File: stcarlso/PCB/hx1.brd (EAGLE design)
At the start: 44.1 x 14 mm, 5 parts, among them J1 SMA_EDGE, J2 CTRL, U1 HX1

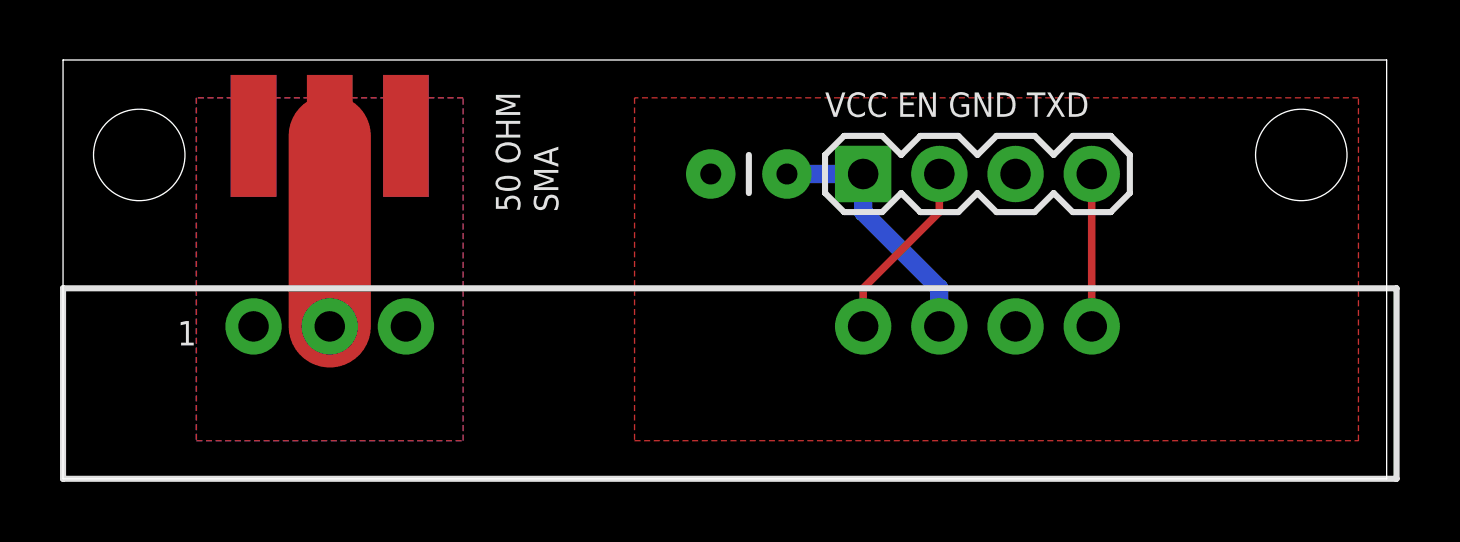
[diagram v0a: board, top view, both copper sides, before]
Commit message: Update PCB to include pads for RC filter (values TBD)
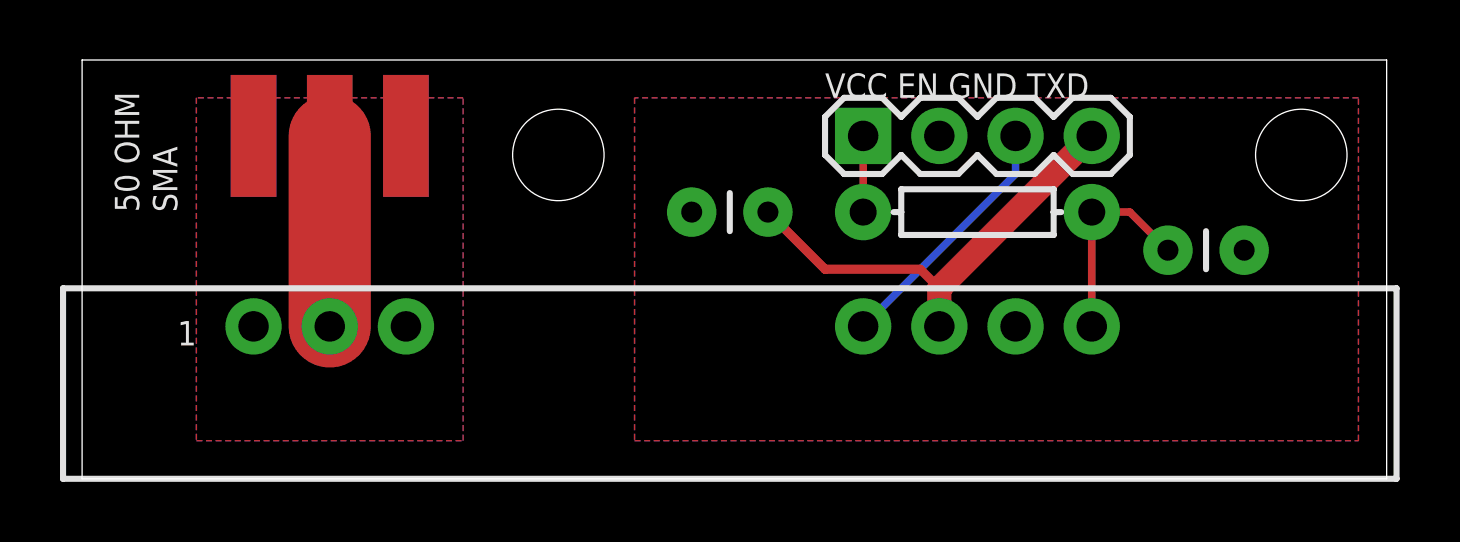
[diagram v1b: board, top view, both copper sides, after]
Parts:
- added C2: TBD, SparkFun-Passives:CAP-PTH-SMALL
- added R1: TBD, SparkFun-Passives:AXIAL-0.3
- moved C1 1.42 mm to (23.5, 8.89)
- moved J2 1.27 mm to (26.7, 11.4)
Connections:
- new net TXF: C2.1, R1.P$1, U1.7
- net EN: now also J2.3; no longer J2.2
- net GND: now also C2.2, J2.2; no longer J2.3
- net TXD: now also J2.1, R1.P$2; no longer J2.4, U1.7
- net VCC: now also J2.4; no longer J2.1
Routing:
- net TXF: track 0.00 -> 6.88 mm
- net VCC: track 8.67 -> 15.2 mm
- net TXD: track 5.08 -> 2.54 mm
- net EN: track 6.13 -> 8.45 mm
- added copper zone on layer 16, net GND
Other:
- board size 44.1 x 14 mm -> 43.5 x 14 mm
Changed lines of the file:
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@@
 <board>
 <plain>
-<wire x1="0" y1="0" x2="44.12" y2="0" width="0" layer="20"/>
+<wire x1="0.635" y1="0" x2="44.12" y2="0" width="0" layer="20"/>
 <wire x1="44.12" y1="0" x2="44.12" y2="13.96" width="0" layer="20"/>
-<wire x1="44.12" y1="13.96" x2="0" y2="13.96" width="0" layer="20"/>
-<wire x1="0" y1="13.96" x2="0" y2="0" width="0" layer="20"/>
-<text x="25.4" y="12.065" size="0.8128" layer="21">VCC EN GND TXD</text>
-<text x="43.18" y="6.985" size="1.27" layer="22" rot="MR0">HAB Project, Microsoft Maker Garage</text>
-<text x="43.18" y="1.905" size="1.27" layer="22" rot="MR0">Revision A, ~STCARLSO</text>
-<text x="15.24" y="8.89" size="0.8128" layer="21" rot="R90">50 OHM</text>
-<text x="16.51" y="8.89" size="0.8128" layer="21" rot="R90">SMA</text>
+<wire x1="44.12" y1="13.96" x2="0.635" y2="13.96" width="0" layer="20"/>
+<wire x1="0.635" y1="13.96" x2="0.635" y2="0" width="0" layer="20"/>
+<text x="25.4" y="12.7" size="0.8128" layer="21">VCC EN GND TXD</text>
+<text x="43.18" y="2.54" size="1.27" layer="22" rot="MR0">HAB Project, Microsoft Maker Garage</text>
+<text x="43.18" y="0.635" size="1.27" layer="22" rot="MR0">Revision A, ~STCARLSO</text>
+<text x="2.54" y="8.89" size="0.8128" layer="21" rot="R90">50 OHM</text>
+<text x="3.81" y="8.89" size="0.8128" layer="21" rot="R90">SMA</text>
 <text x="3.81" y="4.445" size="0.8128" layer="21">1</text>
 <hole x="41.275" y="10.795" drill="3.048"/>
-<hole x="2.54" y="10.795" drill="3.048"/>
+<hole x="16.51" y="10.795" drill="3.048"/>
 </plain>
 <attributes>
@@
 </element>
 <element name="J1" library="SparkFun-Connectors" package="SMA-EDGE" value="SMA_EDGE" x="6.35" y="11.43"/>
-<element name="J2" library="SparkFun-Connectors" package="1X04" value="CTRL" x="26.67" y="10.16" smashed="yes">
-<attribute name="VALUE" x="37.465" y="8.89" size="1.27" layer="27" rot="R90"/>
+<element name="J2" library="SparkFun-Connectors" package="1X04" value="CTRL" x="26.67" y="11.43" smashed="yes">
+<attribute name="VALUE" x="20.32" y="10.795" size="1.27" layer="27"/>
 </element>
 <element name="U1" library="HAB" package="1X12" value="HX1" x="6.35" y="5.08" smashed="yes">
-<attribute name="VALUE" x="1.27" y="0.635" size="1.27" layer="27"/>
-</element>
-<element name="C1" library="SparkFun-Passives" package="CAP-PTH-SMALL" value="0.1u" x="24.13" y="10.16" smashed="yes" rot="R180">
-<attribute name="VALUE" x="23.876" y="12.319" size="0.8128" layer="27" rot="R180"/>
-</element>
+<attribute name="VALUE" x="1.905" y="0.635" size="1.27" layer="27"/>
+</element>
+<element name="C1" library="SparkFun-Passives" package="CAP-PTH-SMALL" value="0.1u" x="23.495" y="8.89" smashed="yes" rot="R180">
+<attribute name="VALUE" x="23.241" y="7.874" size="0.8128" layer="27" rot="R180"/>
+</element>
+<element name="R1" library="SparkFun-Passives" package="AXIAL-0.3" value="TBD" x="30.48" y="8.89" smashed="yes" rot="R180"/>
+<element name="C2" library="SparkFun-Passives" package="CAP-PTH-SMALL" value="TBD" x="36.83" y="7.62" smashed="yes"/>
 </elements>
 <signals>
@@
 <contactref element="U1" pad="1"/>
 <contactref element="U1" pad="3"/>
-<polygon width="0.254" layer="16" isolate="0.3048">
+<polygon width="0.254" layer="16" isolate="0.4064">
 <vertex x="4.445" y="12.7"/>
 <vertex x="4.445" y="1.27"/>
@@
 <vertex x="13.335" y="12.7"/>
 </polygon>
-<polygon width="0.254" layer="1" isolate="0.3048">
+<polygon width="0.254" layer="1" isolate="0.4064">
 <vertex x="4.445" y="12.7"/>
 <vertex x="4.445" y="1.27"/>
@@
 <signal name="EN">
 <contactref element="U1" pad="4"/>
-<contactref element="J2" pad="2"/>
-<wire x1="26.67" y1="5.08" x2="26.67" y2="6.35" width="0.254" layer="1"/>
-<wire x1="26.67" y1="6.35" x2="29.21" y2="8.89" width="0.254" layer="1"/>
-<wire x1="29.21" y1="8.89" x2="29.21" y2="10.16" width="0.254" layer="1"/>
+<contactref element="J2" pad="3"/>
+<wire x1="31.75" y1="11.43" x2="31.75" y2="10.16" width="0.254" layer="16"/>
+<wire x1="31.75" y1="10.16" x2="26.67" y2="5.08" width="0.254" layer="16"/>
 </signal>
 <signal name="VCC">
 <contactref element="U1" pad="5"/>
-<contactref element="J2" pad="1"/>
-<wire x1="29.21" y1="5.08" x2="29.21" y2="6.35" width="0.6096" layer="16"/>
-<wire x1="29.21" y1="6.35" x2="26.67" y2="8.89" width="0.6096" layer="16"/>
-<wire x1="26.67" y1="8.89" x2="26.67" y2="10.16" width="0.6096" layer="16"/>
 <contactref element="C1" pad="1"/>
-<wire x1="24.13" y1="10.16" x2="26.67" y2="10.16" width="0.6096" layer="16"/>
-</signal>
-<signal name="TXD">
-<contactref element="U1" pad="7"/>
 <contactref element="J2" pad="4"/>
-<wire x1="34.29" y1="10.16" x2="34.29" y2="5.08" width="0.254" layer="1"/>
+<wire x1="34.29" y1="11.43" x2="29.21" y2="6.35" width="0.8128" layer="1"/>
+<wire x1="29.21" y1="6.35" x2="29.21" y2="5.08" width="0.8128" layer="1"/>
+<wire x1="29.21" y1="6.35" x2="28.575" y2="6.985" width="0.3048" layer="1"/>
+<wire x1="28.575" y1="6.985" x2="25.4" y2="6.985" width="0.3048" layer="1"/>
+<wire x1="25.4" y1="6.985" x2="23.495" y2="8.89" width="0.3048" layer="1"/>
 </signal>
 <signal name="GND">
 <contactref element="U1" pad="6"/>
-<contactref element="J2" pad="3"/>
 <polygon width="0.254" layer="1" isolate="0.3048">
 <vertex x="19.05" y="12.7"/>
@@
 </polygon>
 <contactref element="C1" pad="2"/>
+<contactref element="C2" pad="2"/>
+<contactref element="J2" pad="2"/>
+<polygon width="0.254" layer="16" isolate="0.3048">
+<vertex x="19.05" y="12.7"/>
+<vertex x="19.05" y="1.27"/>
+<vertex x="43.18" y="1.27"/>
+<vertex x="43.18" y="12.7"/>
+</polygon>
+</signal>
+<signal name="TXF">
+<contactref element="R1" pad="P$1"/>
+<contactref element="C2" pad="1"/>
+<contactref element="U1" pad="7"/>
+<wire x1="34.29" y1="8.89" x2="35.56" y2="8.89" width="0.254" layer="1"/>
+<wire x1="35.56" y1="8.89" x2="36.83" y2="7.62" width="0.254" layer="1"/>
+<wire x1="34.29" y1="8.89" x2="34.29" y2="5.08" width="0.254" layer="1"/>
+</signal>
+<signal name="TXD">
+<contactref element="R1" pad="P$2"/>
+<contactref element="J2" pad="1"/>
+<wire x1="26.67" y1="11.43" x2="26.67" y2="8.89" width="0.254" layer="1"/>
 </signal>
 </signals>

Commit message: Update PCB footprint of HX1 with tighter dimensions
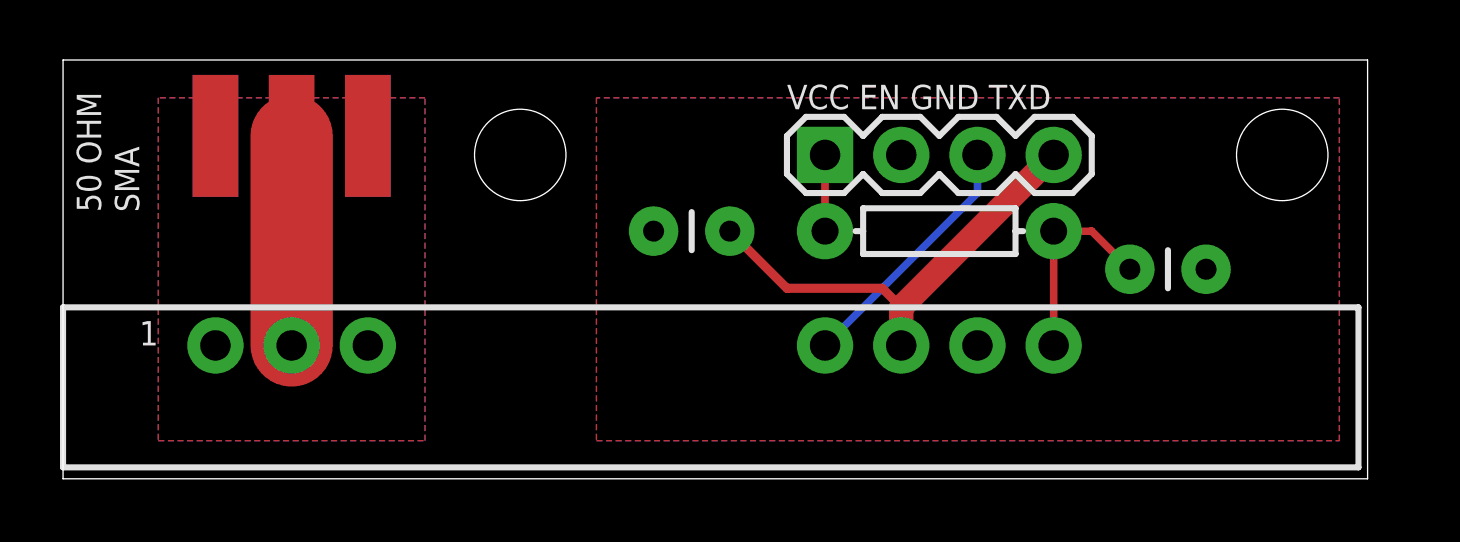
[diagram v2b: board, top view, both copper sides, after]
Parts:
- moved J2 1.42 mm to (25.4, 10.8)
- moved C1 1.42 mm to (22.2, 8.26)
- moved R1 1.42 mm to (29.2, 8.26)
- moved U1 1.42 mm to (5.08, 4.45)
- moved C2 1.42 mm to (35.6, 6.99)
- moved FRAME1 1.27 mm to (-1.27, 15.2)
- moved J1 1.27 mm to (5.08, 11.4)
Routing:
- net RFOUT: track 6.35 -> 6.98 mm
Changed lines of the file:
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@@
 <board>
 <plain>
-<wire x1="0.635" y1="0" x2="44.12" y2="0" width="0" layer="20"/>
-<wire x1="44.12" y1="0" x2="44.12" y2="13.96" width="0" layer="20"/>
-<wire x1="44.12" y1="13.96" x2="0.635" y2="13.96" width="0" layer="20"/>
-<wire x1="0.635" y1="13.96" x2="0.635" y2="0" width="0" layer="20"/>
-<text x="25.4" y="12.7" size="0.8128" layer="21">VCC EN GND TXD</text>
-<text x="43.18" y="2.54" size="1.27" layer="22" rot="MR0">HAB Project, Microsoft Maker Garage</text>
-<text x="43.18" y="0.635" size="1.27" layer="22" rot="MR0">Revision A, ~STCARLSO</text>
-<text x="2.54" y="8.89" size="0.8128" layer="21" rot="R90">50 OHM</text>
-<text x="3.81" y="8.89" size="0.8128" layer="21" rot="R90">SMA</text>
-<text x="3.81" y="4.445" size="0.8128" layer="21">1</text>
-<hole x="41.275" y="10.795" drill="3.048"/>
-<hole x="16.51" y="10.795" drill="3.048"/>
+<wire x1="0" y1="0" x2="43.485" y2="0" width="0" layer="20"/>
+<wire x1="43.485" y1="0" x2="43.485" y2="13.96" width="0" layer="20"/>
+<wire x1="43.485" y1="13.96" x2="0" y2="13.96" width="0" layer="20"/>
+<wire x1="0" y1="13.96" x2="0" y2="0" width="0" layer="20"/>
+<text x="24.13" y="12.319" size="0.8128" layer="21">VCC EN GND TXD</text>
+<text x="41.91" y="2.54" size="1.27" layer="22" rot="MR0">HAB Project, Microsoft Maker Garage</text>
+<text x="41.91" y="0.635" size="1.27" layer="22" rot="MR0">Revision A, ~STCARLSO</text>
+<text x="1.27" y="8.89" size="0.8128" layer="21" rot="R90">50 OHM</text>
+<text x="2.54" y="8.89" size="0.8128" layer="21" rot="R90">SMA</text>
+<text x="2.54" y="4.445" size="0.8128" layer="21">1</text>
+<hole x="40.64" y="10.795" drill="3.048"/>
+<hole x="15.24" y="10.795" drill="3.048"/>
 </plain>
 <attributes>
@@
 </autorouter>
 <elements>
-<element name="FRAME1" library="SparkFun-Aesthetics" package="DUMMY" value="" x="0" y="15.24">
-<attribute name="VERSION" value="v01" x="0" y="15.24" size="1.778" layer="27" display="off"/>
-<attribute name="DESIGNER" value="Nobody" x="0" y="15.24" size="1.778" layer="27" display="off"/>
-</element>
-<element name="J1" library="SparkFun-Connectors" package="SMA-EDGE" value="SMA_EDGE" x="6.35" y="11.43"/>
-<element name="J2" library="SparkFun-Connectors" package="1X04" value="CTRL" x="26.67" y="11.43" smashed="yes">
-<attribute name="VALUE" x="20.32" y="10.795" size="1.27" layer="27"/>
-</element>
-<element name="U1" library="HAB" package="1X12" value="HX1" x="6.35" y="5.08" smashed="yes">
-<attribute name="VALUE" x="1.905" y="0.635" size="1.27" layer="27"/>
-</element>
-<element name="C1" library="SparkFun-Passives" package="CAP-PTH-SMALL" value="0.1u" x="23.495" y="8.89" smashed="yes" rot="R180">
-<attribute name="VALUE" x="23.241" y="7.874" size="0.8128" layer="27" rot="R180"/>
-</element>
-<element name="R1" library="SparkFun-Passives" package="AXIAL-0.3" value="TBD" x="30.48" y="8.89" smashed="yes" rot="R180"/>
-<element name="C2" library="SparkFun-Passives" package="CAP-PTH-SMALL" value="TBD" x="36.83" y="7.62" smashed="yes"/>
+<element name="FRAME1" library="SparkFun-Aesthetics" package="DUMMY" value="" x="-1.27" y="15.24">
+<attribute name="VERSION" value="v01" x="-1.27" y="15.24" size="1.778" layer="27" display="off"/>
+<attribute name="DESIGNER" value="Nobody" x="-1.27" y="15.24" size="1.778" layer="27" display="off"/>
+</element>
+<element name="J1" library="SparkFun-Connectors" package="SMA-EDGE" value="SMA_EDGE" x="5.08" y="11.43"/>
+<element name="J2" library="SparkFun-Connectors" package="1X04" value="CTRL" x="25.4" y="10.795" smashed="yes">
+<attribute name="VALUE" x="19.05" y="10.16" size="1.27" layer="27"/>
+</element>
+<element name="U1" library="HAB" package="1X12" value="HX1" x="5.08" y="4.445" smashed="yes">
+<attribute name="VALUE" x="0.635" y="1.27" size="1.27" layer="27"/>
+</element>
+<element name="C1" library="SparkFun-Passives" package="CAP-PTH-SMALL" value="0.1u" x="22.225" y="8.255" smashed="yes" rot="R180">
+<attribute name="VALUE" x="21.971" y="7.239" size="0.8128" layer="27" rot="R180"/>
+</element>
+<element name="R1" library="SparkFun-Passives" package="AXIAL-0.3" value="TBD" x="29.21" y="8.255" smashed="yes" rot="R180"/>
+<element name="C2" library="SparkFun-Passives" package="CAP-PTH-SMALL" value="TBD" x="35.56" y="6.985" smashed="yes"/>
 </elements>
 <signals>
@@
 <contactref element="J1" pad="SIG"/>
 <contactref element="U1" pad="2"/>
-<wire x1="8.89" y1="11.43" x2="8.89" y2="5.08" width="2.7432" layer="1"/>
+<wire x1="7.62" y1="11.43" x2="7.62" y2="4.445" width="2.7432" layer="1"/>
 </signal>
 <signal name="RFGND">
@@
 <contactref element="U1" pad="3"/>
 <polygon width="0.254" layer="16" isolate="0.4064">
-<vertex x="4.445" y="12.7"/>
-<vertex x="4.445" y="1.27"/>
-<vertex x="13.335" y="1.27"/>
-<vertex x="13.335" y="12.7"/>
+<vertex x="3.175" y="12.7"/>
+<vertex x="3.175" y="1.27"/>
+<vertex x="12.065" y="1.27"/>
+<vertex x="12.065" y="12.7"/>
 </polygon>
 <polygon width="0.254" layer="1" isolate="0.4064">
-<vertex x="4.445" y="12.7"/>
-<vertex x="4.445" y="1.27"/>
-<vertex x="13.335" y="1.27"/>
-<vertex x="13.335" y="12.7"/>
+<vertex x="3.175" y="12.7"/>
+<vertex x="3.175" y="1.27"/>
+<vertex x="12.065" y="1.27"/>
+<vertex x="12.065" y="12.7"/>
 </polygon>
 </signal>
@@
 <contactref element="U1" pad="4"/>
 <contactref element="J2" pad="3"/>
-<wire x1="31.75" y1="11.43" x2="31.75" y2="10.16" width="0.254" layer="16"/>
-<wire x1="31.75" y1="10.16" x2="26.67" y2="5.08" width="0.254" layer="16"/>
+<wire x1="30.48" y1="10.795" x2="30.48" y2="9.525" width="0.254" layer="16"/>
+<wire x1="30.48" y1="9.525" x2="25.4" y2="4.445" width="0.254" layer="16"/>
 </signal>
 <signal name="VCC">
@@
 <contactref element="C1" pad="1"/>
 <contactref element="J2" pad="4"/>
-<wire x1="34.29" y1="11.43" x2="29.21" y2="6.35" width="0.8128" layer="1"/>
-<wire x1="29.21" y1="6.35" x2="29.21" y2="5.08" width="0.8128" layer="1"/>
-<wire x1="29.21" y1="6.35" x2="28.575" y2="6.985" width="0.3048" layer="1"/>
-<wire x1="28.575" y1="6.985" x2="25.4" y2="6.985" width="0.3048" layer="1"/>
-<wire x1="25.4" y1="6.985" x2="23.495" y2="8.89" width="0.3048" layer="1"/>
+<wire x1="33.02" y1="10.795" x2="27.94" y2="5.715" width="0.8128" layer="1"/>
+<wire x1="27.94" y1="5.715" x2="27.94" y2="4.445" width="0.8128" layer="1"/>
+<wire x1="27.94" y1="5.715" x2="27.305" y2="6.35" width="0.3048" layer="1"/>
+<wire x1="27.305" y1="6.35" x2="24.13" y2="6.35" width="0.3048" layer="1"/>
+<wire x1="24.13" y1="6.35" x2="22.225" y2="8.255" width="0.3048" layer="1"/>
 </signal>
 <signal name="GND">
 <contactref element="U1" pad="6"/>
 <polygon width="0.254" layer="1" isolate="0.3048">
-<vertex x="19.05" y="12.7"/>
-<vertex x="19.05" y="1.27"/>
-<vertex x="43.18" y="1.27"/>
-<vertex x="43.18" y="12.7"/>
+<vertex x="17.78" y="12.7"/>
+<vertex x="17.78" y="1.27"/>
+<vertex x="42.545" y="1.27"/>
+<vertex x="42.545" y="12.7"/>
 </polygon>
 <contactref element="C1" pad="2"/>
@@
 <contactref element="J2" pad="2"/>
 <polygon width="0.254" layer="16" isolate="0.3048">
-<vertex x="19.05" y="12.7"/>
-<vertex x="19.05" y="1.27"/>
-<vertex x="43.18" y="1.27"/>
-<vertex x="43.18" y="12.7"/>
+<vertex x="17.78" y="12.7"/>
+<vertex x="17.78" y="1.27"/>
+<vertex x="42.545" y="1.27"/>
+<vertex x="42.545" y="12.7"/>
 </polygon>
 </signal>
@@
 <contactref element="C2" pad="1"/>
 <contactref element="U1" pad="7"/>
-<wire x1="34.29" y1="8.89" x2="35.56" y2="8.89" width="0.254" layer="1"/>
-<wire x1="35.56" y1="8.89" x2="36.83" y2="7.62" width="0.254" layer="1"/>
-<wire x1="34.29" y1="8.89" x2="34.29" y2="5.08" width="0.254" layer="1"/>
+<wire x1="33.02" y1="8.255" x2="34.29" y2="8.255" width="0.254" layer="1"/>
+<wire x1="34.29" y1="8.255" x2="35.56" y2="6.985" width="0.254" layer="1"/>
+<wire x1="33.02" y1="8.255" x2="33.02" y2="4.445" width="0.254" layer="1"/>
 </signal>
 <signal name="TXD">
 <contactref element="R1" pad="P$2"/>
 <contactref element="J2" pad="1"/>
-<wire x1="26.67" y1="11.43" x2="26.67" y2="8.89" width="0.254" layer="1"/>
+<wire x1="25.4" y1="10.795" x2="25.4" y2="8.255" width="0.254" layer="1"/>
 </signal>
 </signals>
